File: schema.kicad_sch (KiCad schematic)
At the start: 7 parts, among them U1 74HC595D, U2 74HC595D, U5 AT28C256-15PU

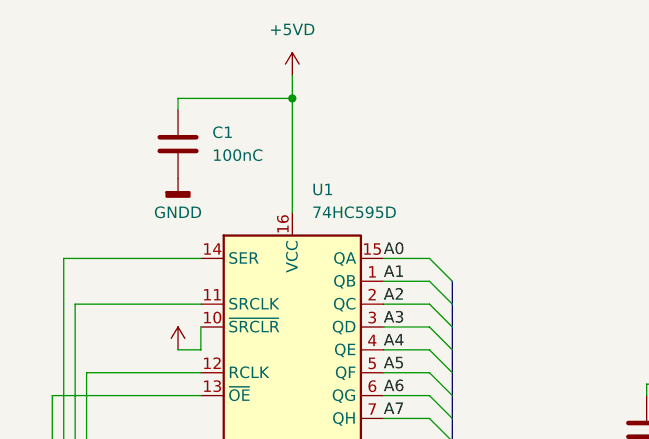
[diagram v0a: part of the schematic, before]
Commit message: update condensators
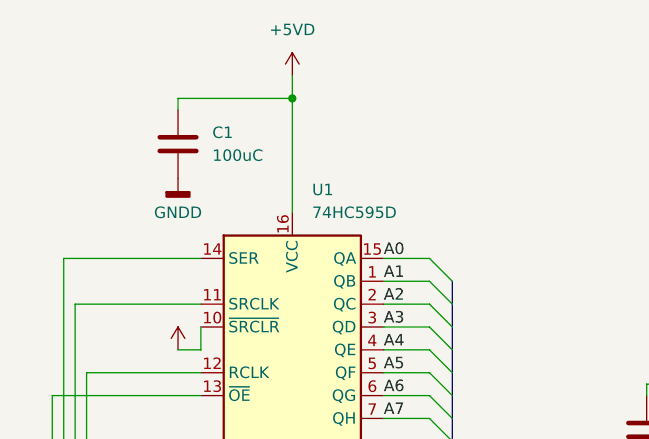
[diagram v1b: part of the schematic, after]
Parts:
- C1: value 100nC -> 100uC
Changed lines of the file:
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@@
       (effects (font (size 1.27 1.27)) (justify left))
     )
-    (property "Value" "100nC" (at 80.01 57.15 0)
+    (property "Value" "100uC" (at 80.01 57.15 0)
       (effects (font (size 1.27 1.27)) (justify left))
     )

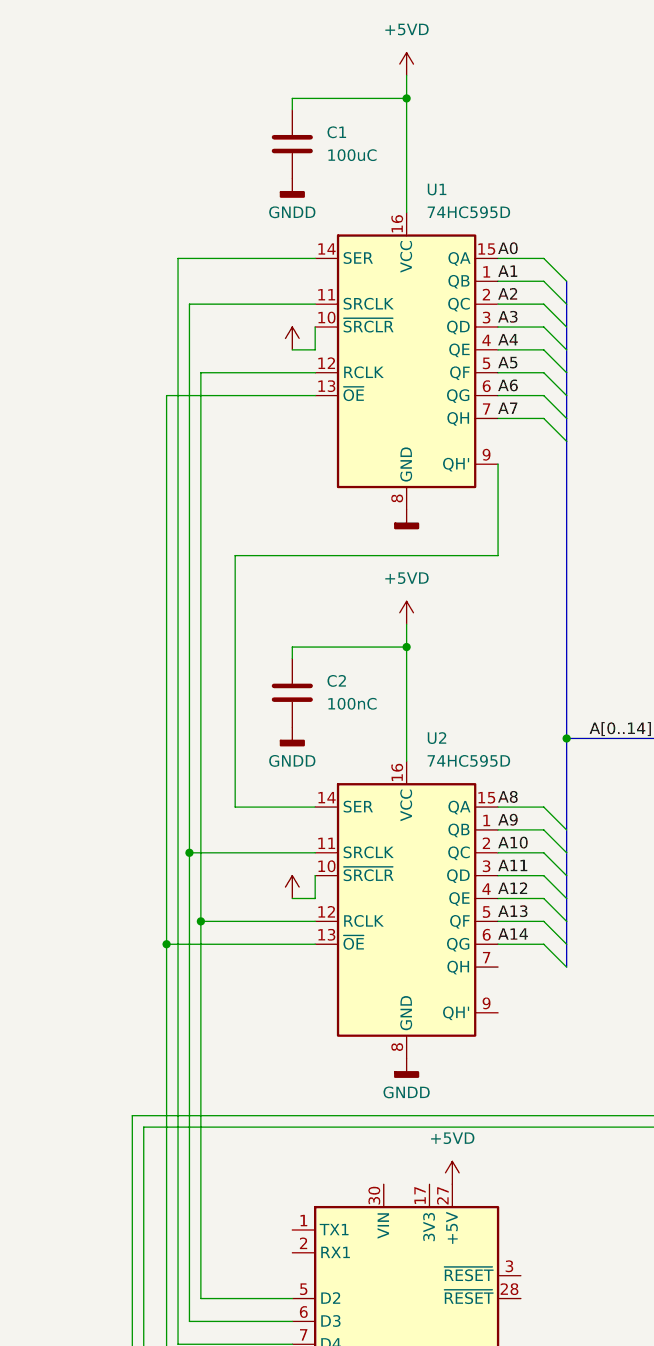
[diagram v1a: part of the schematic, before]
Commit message: update capacitor to 10uC
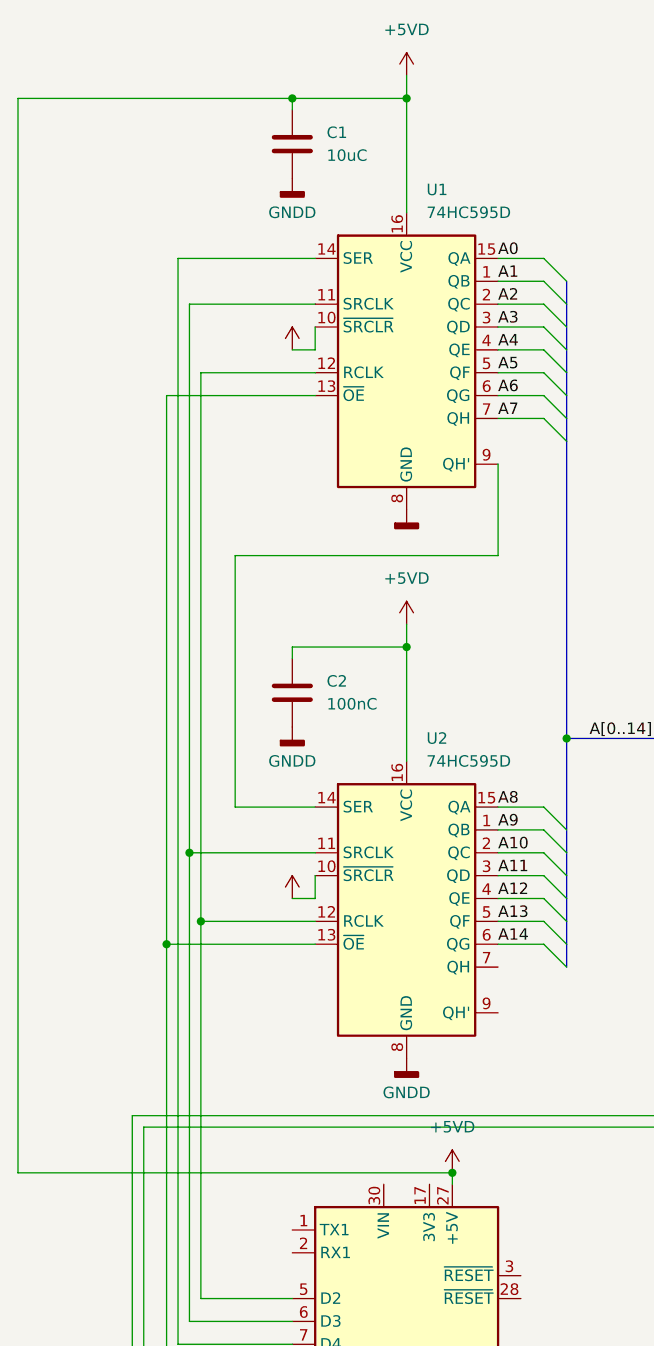
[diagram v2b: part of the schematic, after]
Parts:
- C1: value 100uC -> 10uC
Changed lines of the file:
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@@
   (junction (at 62.23 144.78) (diameter 0) (color 0 0 0 0)
   )
+  (junction (at 93.98 170.18) (diameter 0) (color 0 0 0 0)
+  )
   (junction (at 66.04 142.24) (diameter 0) (color 0 0 0 0)
   )
+  (junction (at 76.2 50.8) (diameter 0) (color 0 0 0 0)
+  )
   (junction (at 64.77 134.62) (diameter 0) (color 0 0 0 0)
   )
@@
     (stroke (width 0) (type default))
   )
+  (wire (pts (xy 93.98 170.18) (xy 45.72 170.18))
+    (stroke (width 0) (type default))
+  )
   (bus (pts (xy 156.21 105.41) (xy 156.21 107.95))
     (stroke (width 0) (type default))
@@
     (stroke (width 0) (type default))
   )
+  (wire (pts (xy 45.72 170.18) (xy 45.72 50.8))
+    (stroke (width 0) (type default))
+  )
   (wire (pts (xy 99.06 132.08) (xy 104.14 132.08))
     (stroke (width 0) (type default))
@@
     (stroke (width 0) (type default))
   )
+  (wire (pts (xy 93.98 170.18) (xy 93.98 171.45))
+    (stroke (width 0) (type default))
+  )
   (wire (pts (xy 123.19 107.95) (xy 130.81 107.95))
     (stroke (width 0) (type default))
@@
   )
   (wire (pts (xy 76.2 111.76) (xy 76.2 113.03))
+    (stroke (width 0) (type default))
+  )
+  (wire (pts (xy 45.72 50.8) (xy 76.2 50.8))
     (stroke (width 0) (type default))
   )
@@
       (effects (font (size 1.27 1.27)) (justify left))
     )
-    (property "Value" "100uC" (at 80.01 57.15 0)
+    (property "Value" "10uC" (at 80.01 57.15 0)
       (effects (font (size 1.27 1.27)) (justify left))
     )
@@
     )
   )
-  (symbol (lib_id "power:+5VD") (at 93.98 171.45 0) (unit 1)
+  (symbol (lib_id "power:+5VD") (at 93.98 170.18 0) (unit 1)
     (in_bom yes) (on_board yes) (dnp no) (fields_autoplaced)
-    (property "Reference" "#PWR04" (at 93.98 175.26 0)
-      (effects (font (size 1.27 1.27)) hide)
-    )
-    (property "Value" "+5VD" (at 93.98 166.37 0)
+    (property "Reference" "#PWR04" (at 93.98 173.99 0)
+      (effects (font (size 1.27 1.27)) hide)
+    )
+    (property "Value" "+5VD" (at 93.98 165.1 0)
       (effects (font (size 1.27 1.27)))
     )
-    (property "Footprint" "" (at 93.98 171.45 0)
-      (effects (font (size 1.27 1.27)) hide)
-    )
-    (property "Datasheet" "" (at 93.98 171.45 0)
-      (effects (font (size 1.27 1.27)) hide)
-    )
+    (property "Footprint" "" (at 93.98 170.18 0)
+      (effects (font (size 1.27 1.27)) hide)
+    )
+    (property "Datasheet" "" (at 93.98 170.18 0)
+      (effects (font (size 1.27 1.27)) hide)
+    )

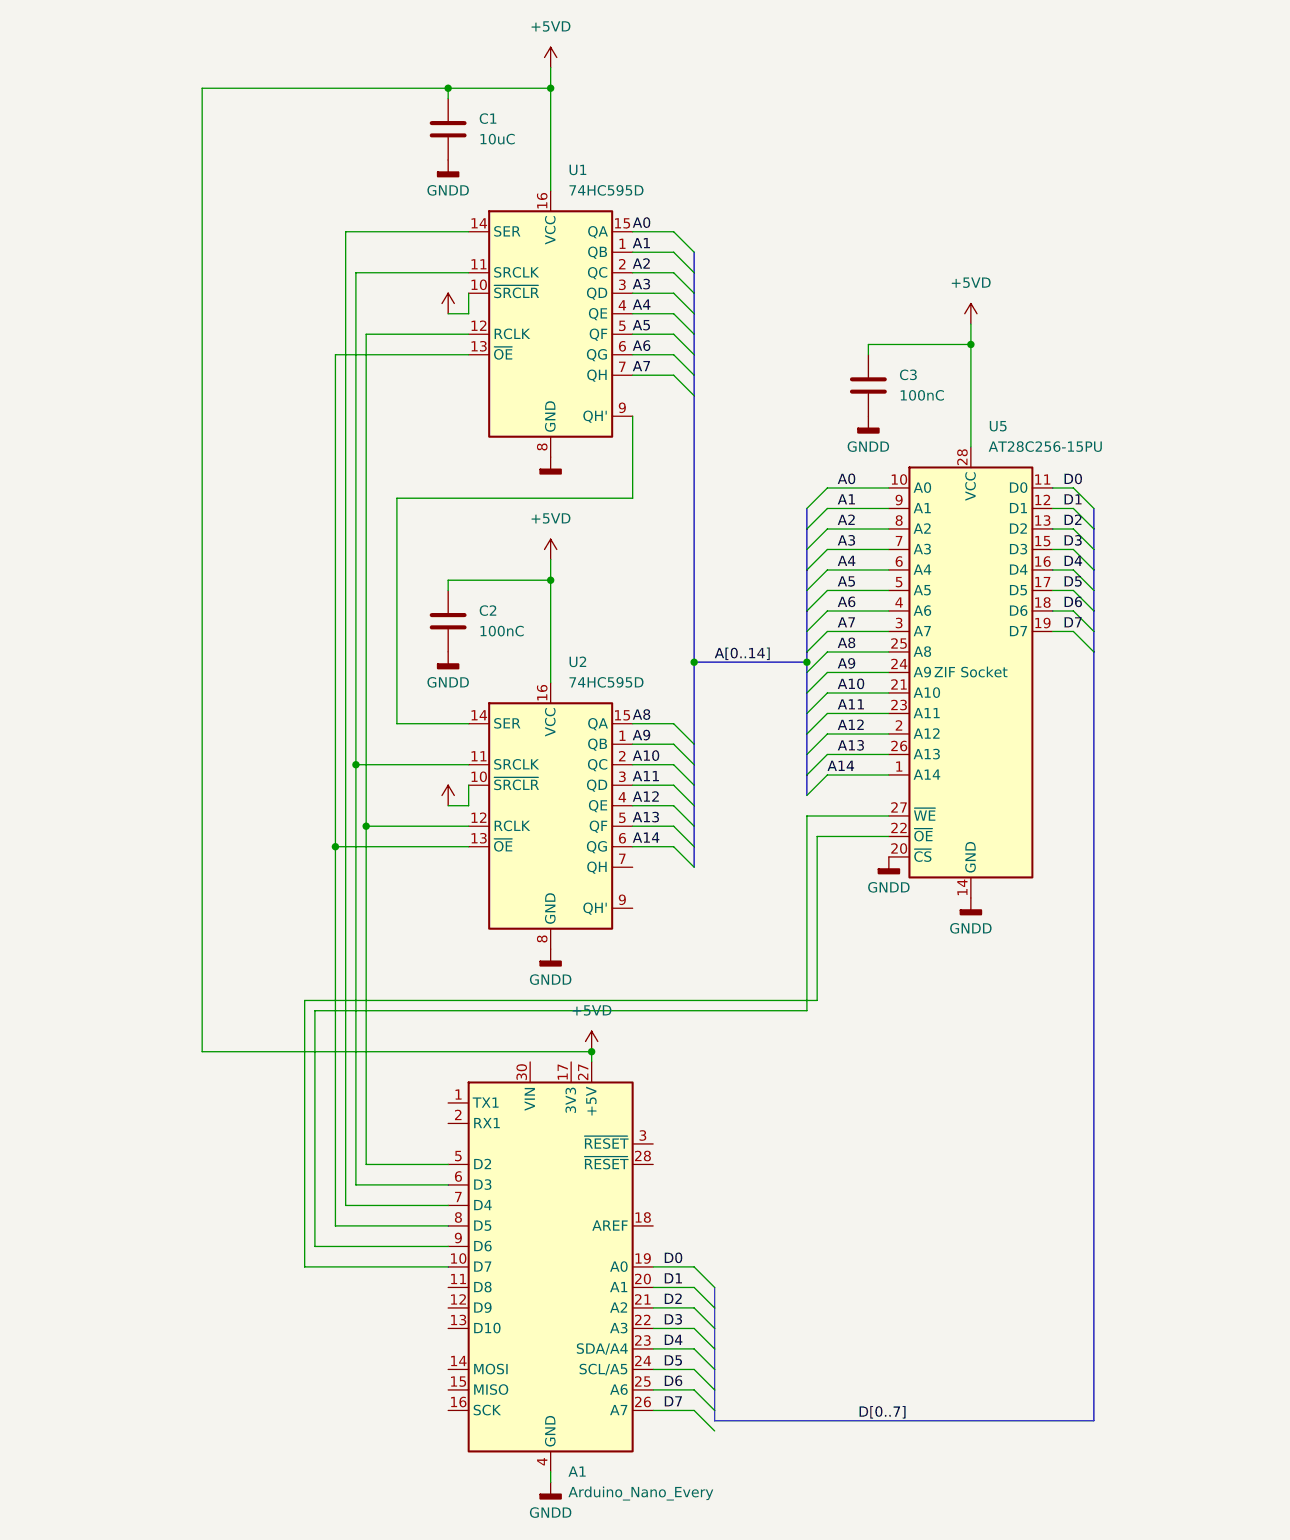
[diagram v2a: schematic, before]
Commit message: reroute eeprom cs to arduino
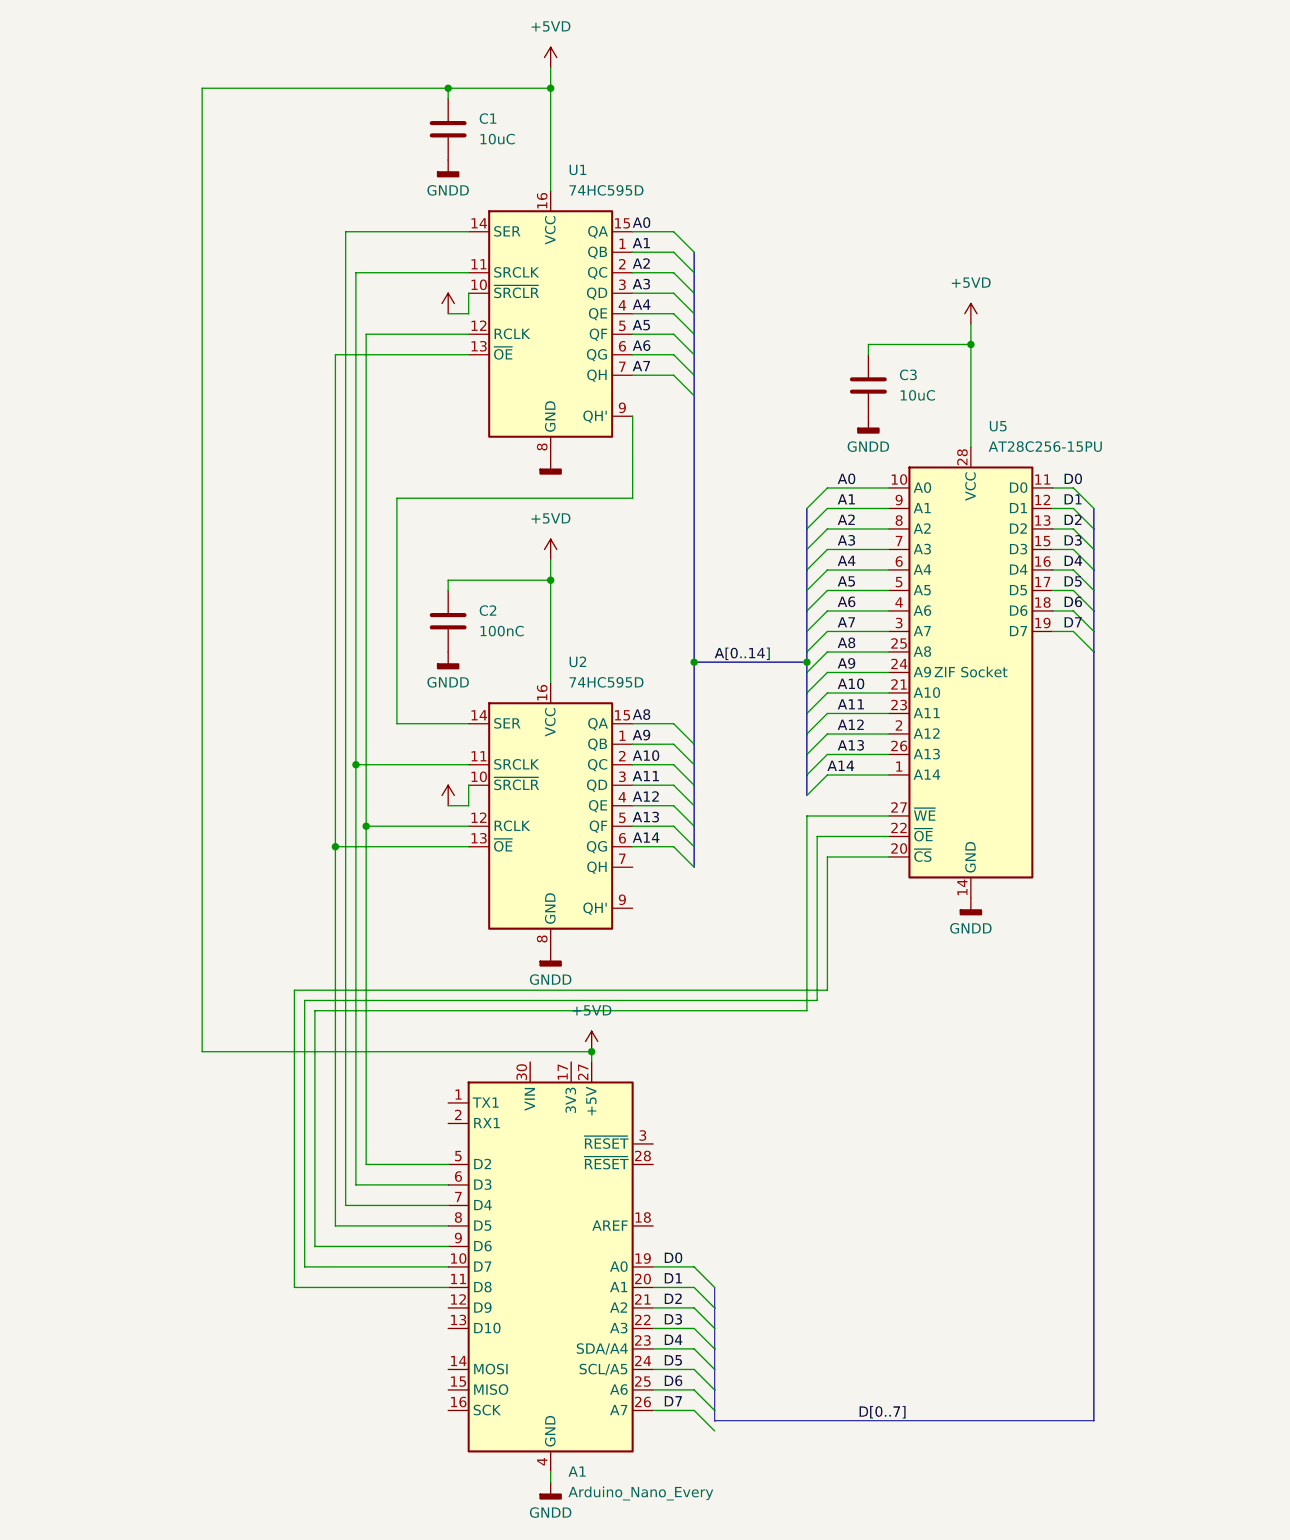
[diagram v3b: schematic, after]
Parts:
- C3: value 100nC -> 10uC
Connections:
- net GNDD: no longer U5.20 (~{CS})
- net at A1.11 (D8): now also U5.20 (~{CS})
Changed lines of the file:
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@@
+    (stroke (width 0) (type default))
+  )
+  (wire (pts (xy 57.15 162.56) (xy 57.15 199.39))
     (stroke (width 0) (type default))
   )
@@
     (stroke (width 0) (type default))
   )
+  (wire (pts (xy 123.19 162.56) (xy 57.15 162.56))
+    (stroke (width 0) (type default))
+  )
   (wire (pts (xy 151.13 107.95) (xy 153.67 107.95))
     (stroke (width 0) (type default))
@@
     (stroke (width 0) (type default))
   )
+  (wire (pts (xy 130.81 146.05) (xy 123.19 146.05))
+    (stroke (width 0) (type default))
+  )
   (wire (pts (xy 69.85 101.6) (xy 99.06 101.6))
     (stroke (width 0) (type default))
@@
     (stroke (width 0) (type default))
   )
+  (wire (pts (xy 123.19 146.05) (xy 123.19 162.56))
+    (stroke (width 0) (type default))
+  )
   (bus (pts (xy 120.65 130.81) (xy 120.65 133.35))
     (stroke (width 0) (type default))
@@
   )
   (wire (pts (xy 151.13 110.49) (xy 153.67 110.49))
+    (stroke (width 0) (type default))
+  )
+  (wire (pts (xy 57.15 199.39) (xy 76.2 199.39))
     (stroke (width 0) (type default))
   )
@@
       (effects (font (size 1.27 1.27)) (justify left))
     )
-    (property "Value" "100nC" (at 132.08 88.9 0)
+    (property "Value" "10uC" (at 132.08 88.9 0)
       (effects (font (size 1.27 1.27)) (justify left))
     )
@@
         )
       )
-    )
-  )
-  (symbol (lib_id "power:GNDD") (at 130.81 146.05 0) (unit 1)
-    (in_bom yes) (on_board yes) (dnp no) (fields_autoplaced)
-    (property "Reference" "#PWR010" (at 130.81 152.4 0)
-      (effects (font (size 1.27 1.27)) hide)
-    )
-    (property "Value" "GNDD" (at 130.81 149.86 0)
-      (effects (font (size 1.27 1.27)))
-    )
-    (property "Footprint" "" (at 130.81 146.05 0)
-      (effects (font (size 1.27 1.27)) hide)
-    )
-    (property "Datasheet" "" (at 130.81 146.05 0)
-      (effects (font (size 1.27 1.27)) hide)
-    )
-    (pin "1")
-    (instances
-      (project "schema"
-        (path "/7e7dcb81-504a-48dc-946a-8711b32d05eb"
-          (reference "#PWR010") (unit 1)
-        )
-      )
